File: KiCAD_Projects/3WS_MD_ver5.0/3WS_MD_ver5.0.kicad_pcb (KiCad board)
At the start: 2 copper layers, 80 x 100 mm, 149 parts, among them P1 CONN_01X02, P10 CONN_01X04, P11 TST, P12 CONN_02X08, P13 CONN_01X06, P14 CONN_01X02, P15 CONN_01X02, P16 CONN_01X04, P17 CONN_01X04, P2 CONN_01X02, P20 CONN_01X03, P3 CONN_01X04, P4 CONN_02X06, P5 TST, P6 CONN_01X04, P7 CONN_01X02, P8 CONN_01X04, P9 TST, Q1 MOSFET_N, Q2 MOSFET_N, Q3 MOSFET_N, Q4 MOSFET_N, Q5 MOSFET_N, Q6 MOSFET_N, Q7 MOSFET_N, Q8 MOSFET_N, SW1 SW_PUSH, SW2 SW_PUSH, SW3 SW_PUSH, U1 STM32F103_48, U10 NCP1117ST33T3G, U11 TBD62083A, U2 SI8234, U3 SI8234, U4 LM7812, U5 SI8234, U6 SI8234, U7 7805, U8 MAX3051, U9 SW_ROTARY_16, X2 CRYSTAL

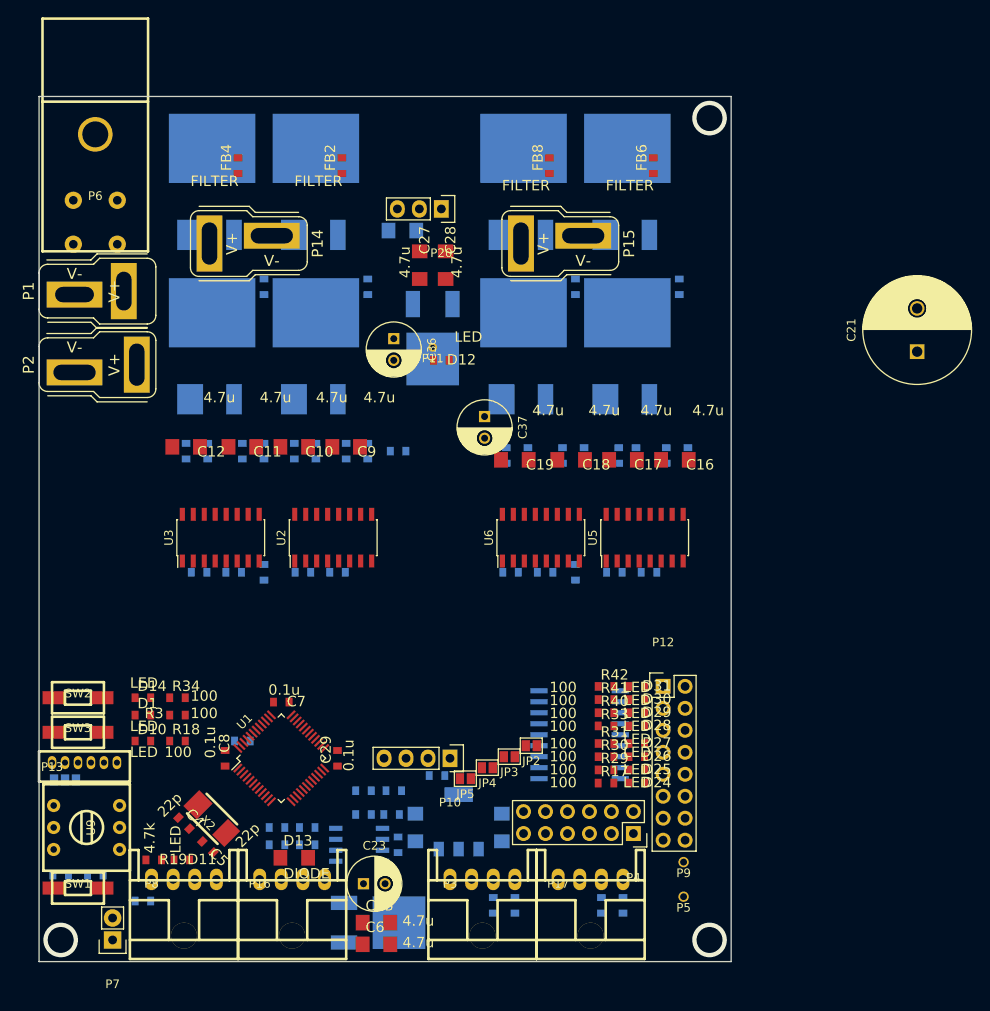
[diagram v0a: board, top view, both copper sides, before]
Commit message: ver5.0と5.0Exの設計終わり｡CAN node ver1.2の設計終わり｡BLMD基板設計開始｡ISO_DCDCver1.1設計開始｡
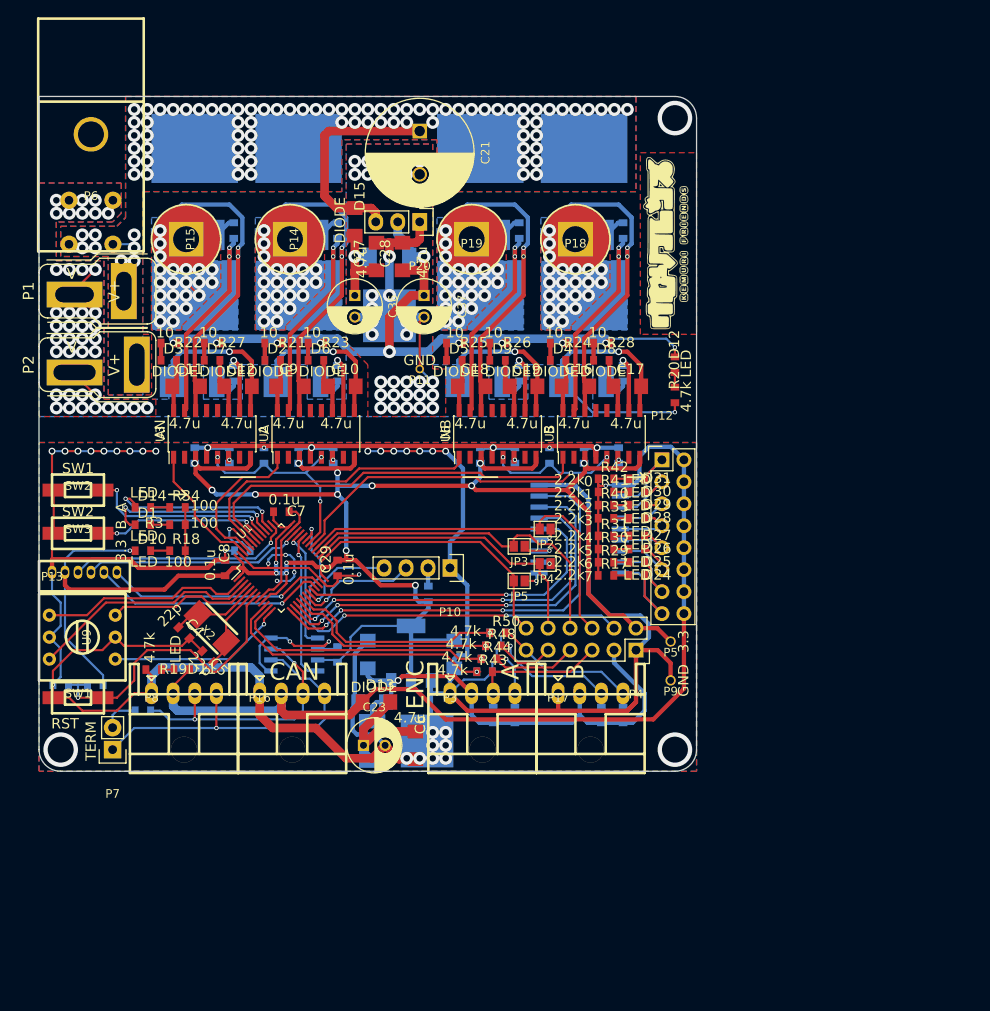
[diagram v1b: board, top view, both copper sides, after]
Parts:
- removed JP1: JUMPER3, Connect:GS3
- added G***: LOGO, Symbols:kemuhure_reg, F.Cu at (72.5, 17.0)
- added G***: LOGO, Symbols:kemuhure, F.Cu at (72.5, 17.0)
- added P18: CONN_01X01, RP_KiCAD_Connector:KRB-300, F.Cu at (62.0, 16.5)
- added P19: CONN_01X01, RP_KiCAD_Connector:KRB-300, F.Cu at (50.0, 16.5)
- C13, FB2, FB4, FB6, FB8: moved to B.Cu
- D15, D2, D3, D4, D5, D6, D7, D8, D9, R20, R21, R22, R23, R24, R25, R26, R27, R28, R43, R44, R48, R50: moved to F.Cu
- P14, P15: value CONN_01X02 -> CONN_01X01; footprint RP_KiCAD_Connector:DEANS_T_F -> RP_KiCAD_Connector:KRB-300
- R17, R29, R30, R31, R33, R40, R41, R42: value 100 -> 2.2k
- moved C21 62.9 mm to (44.0, 4.00), turned to 270 degrees
- moved P15 43.0 mm to (17.0, 16.5)
- moved R20 32.7 mm to (73.5, 34.5), turned to 270 degrees
- moved R46 31.3 mm to (52.0, 65.0), turned to 180 degrees
- moved R45 31.2 mm to (51.5, 66.5), turned to 180 degrees
- moved P5 29.5 mm to (73.0, 63.0)
- moved R44 28.7 mm to (52.0, 65.0)
- moved R43 28.6 mm to (51.5, 66.5)
- moved D12 27.0 mm to (73.5, 31.0), turned to 270 degrees
- moved P12 26.2 mm to (72.0, 42.0)
- moved C13 25.5 mm to (38.5, 70.0), turned to 180 degrees
- moved JP2 25.1 mm to (58.5, 50.0)
- moved R47 24.6 mm to (52.5, 63.5), turned to 180 degrees
- moved JP4 24.5 mm to (58.5, 54.0)
- moved JP3 24.3 mm to (55.5, 52.0)
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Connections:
- P13 pad 2: Net-(JP1-Pad2) -> +3.3V
- P14 pad 1: /OUT_AN -> /OUT_A
- P15 pad 1: /OUT_BN -> /OUT_AN
- P4 pad 11: /ENC_Ba -> /ENC_Bb
- P4 pad 9: /ENC_Bb -> /ENC_Ba
- R36 pad 1: +3.3V -> +5V
- R37 pad 1: +3.3V -> +5V
- R38 pad 1: +3.3V -> +5V
- R39 pad 1: +3.3V -> +5V
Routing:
- net GND: track 0.00 -> 442.1 mm, vias 0 -> 39
- net +3.3V: track 0.00 -> 248.2 mm, vias 0 -> 17
- net GNDPWR: track 0.00 -> 243.6 mm, vias 0 -> 79
- net +BATT: track 0.00 -> 151.9 mm, vias 0 -> 84
- net +12V: track 0.00 -> 124.1 mm, vias 0 -> 1
- net /OUT_BN: track 0.00 -> 101.9 mm, vias 0 -> 24
- net /GD_12V: track 0.00 -> 91.1 mm, vias 0 -> 11
- net /OUT_A: track 0.00 -> 89.1 mm, vias 0 -> 24
- net /OUT_B: track 0.00 -> 83.0 mm, vias 0 -> 24
- net /OUT_AN: track 0.00 -> 79.8 mm, vias 0 -> 24
- net +5V: track 0.00 -> 55.6 mm, vias 0 -> 1
- net /VALVE_0: track 0.00 -> 51.1 mm, vias 0 -> 3
- net /V_RX: track 0.00 -> 50.1 mm, vias 0 -> 3
- net /MOTORB_EN: track 0.00 -> 49.7 mm, vias 0 -> 3
- net /VALVE_1: track 0.00 -> 47.8 mm, vias 0 -> 3
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- added copper zone on F.Cu, net (none)
- added copper zone on B.Cu, net +BATT
- added copper zone on F.Cu, net +BATT
- added copper zone on B.Cu, net /OUT_A
- added copper zone on F.Cu, net /OUT_A
- added copper zone on B.Cu, net /OUT_AN
- added copper zone on F.Cu, net /OUT_AN
- added copper zone on B.Cu, net /OUT_B
- added copper zone on F.Cu, net /OUT_B
- added copper zone on B.Cu, net /OUT_BN
- added copper zone on F.Cu, net /OUT_BN
- added copper zone on B.Cu, net GND
- added copper zone on F.Cu, net GND
- added copper zone on B.Cu, net GNDPWR
- added copper zone on F.Cu, net GNDPWR
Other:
- board size 80 x 100 mm -> 76 x 78 mm
- board text added: "0"
- board text added: "1"
- board text added: "2"
- board text added: "3"
- board text added: "3.3"
- board text added: "4"
- board text added: "5"
- board text added: "6"
- board text added: "7"
- board text added: "A"
- board text added: "AN"
- board text added: "B"
- board text added: "CAN"
- board text added: "ENC"
- board text added: "GND"
- board text added: "NB"
- board text added: "RST"
- board text added: "SW1"
- board text added: "SW2"
- board text added: "TERM"

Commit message: セルチェッカー作った｡電源基板ver1.1作った｡ぶっさしMDいじった｡DCDCいじりだした｡
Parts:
- moved D12 3.00 mm to (73.5, 34.0), turned to 0 degrees
- moved R20 1.50 mm to (73.5, 36.0), turned to 180 degrees
- moved G*** 0.50 mm to (72.5, 17.5) (x2)
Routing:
- net /GD_12V: track 91.1 -> 93.2 mm
